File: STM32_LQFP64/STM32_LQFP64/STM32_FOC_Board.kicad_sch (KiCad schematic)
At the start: 37 parts, among them J1 Bus_M.2_Socket_E, SW1 TS342A2P-WZ, SW2 TS342A2P-WZ, U1 STM32F446RETx, U2 ME6217C33M5G, X1 FC-12M32.768KHZ7PF20PPM, X2 7R24000E12UBE

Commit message: update L431
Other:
- note added: "STM32F401xx STM32F410xx STM32F411xx STM32F412xx STM32F413xx STM32F423xx STM32F446xx STM32L431xx :"
- note removed: "STM32F401xx STM32F410xx STM32F411xx STM32F412xx STM32F413xx STM32F423xx STM32F446xx :"
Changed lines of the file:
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@@
     (effects (font (size 2.54 2.54)) (justify left bottom))
   )
-  (text "STM32F401xx\nSTM32F410xx\nSTM32F411xx\nSTM32F412xx\nSTM32F413xx\nSTM32F423xx\nSTM32F446xx  :\n"
+  (text "STM32F401xx\nSTM32F410xx\nSTM32F411xx\nSTM32F412xx\nSTM32F413xx\nSTM32F423xx\nSTM32F446xx\nSTM32L431xx  :\n"
     (at 121.92 167.64 0)
     (effects (font (size 1.27 1.27)) (justify left bottom))

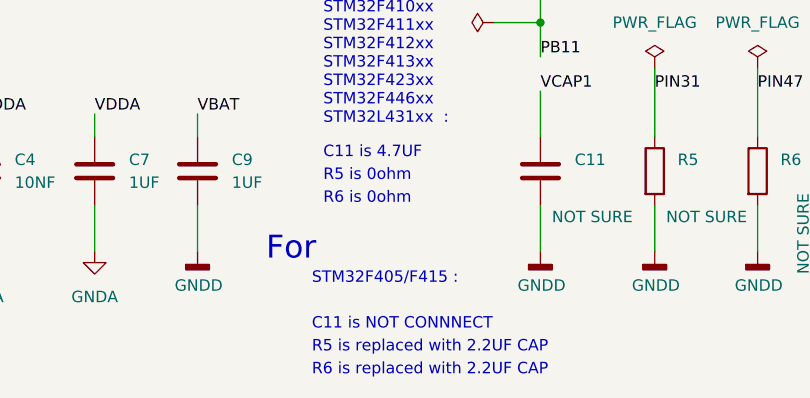
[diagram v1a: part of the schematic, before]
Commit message: update L051
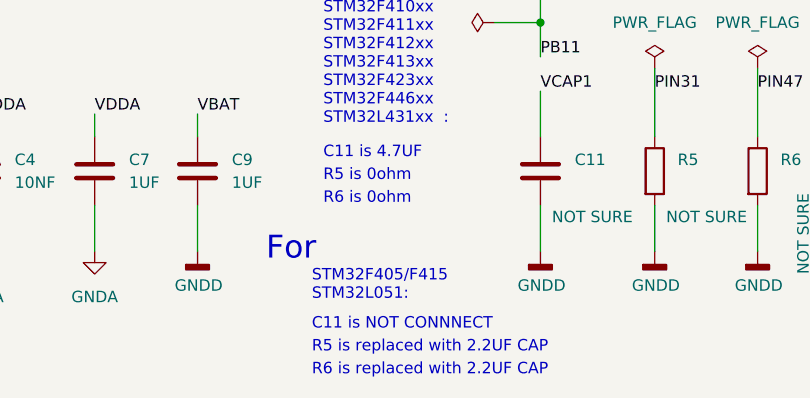
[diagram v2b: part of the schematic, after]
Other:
- note added: "STM32F405/F415 STM32L051:"
- note removed: "STM32F405/F415 :"
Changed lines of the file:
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@@
     (effects (font (size 1.27 1.27)) (justify left bottom))
   )
-  (text "STM32F405/F415 :" (at 120.65 185.42 0)
+  (text "STM32F405/F415\nSTM32L051:" (at 120.65 187.198 0)
     (effects (font (size 1.27 1.27)) (justify left bottom))
   )
